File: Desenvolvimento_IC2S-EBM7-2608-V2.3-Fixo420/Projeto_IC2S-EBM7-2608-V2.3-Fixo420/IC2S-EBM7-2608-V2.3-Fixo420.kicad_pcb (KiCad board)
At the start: 4 copper layers, 60 x 60 mm, 148 parts, among them P1 M20-7822046, P2 M20-7821446, T1 TP_+24V, T2 TP_GND_ADC_P1, T3 TP_DGND, T4 TP_+5V_REG, T5 TP_+3.3V_DIG, T6 TP_+3.3V_ANA, T7 TP_GND_ADC, T8 TP_+24V_ADC, U1 R-78HB5.0-0.5L, U10 TPS26613DDFR, U11 TPS26613DDFR, U12 TPS7A4001DGN, U13 LP5907MFX-2.5, U2 MCP1824ST-3302E/DB, U3 SPX3819M5-L-3-3/TR, U4 TL431B, U5 ISO7141CCDBQR, U6 AD7124-8BCPZ, U7 ADR4525BRZ, U8 TPS26613DDFR, U9 TPS26613DDFR

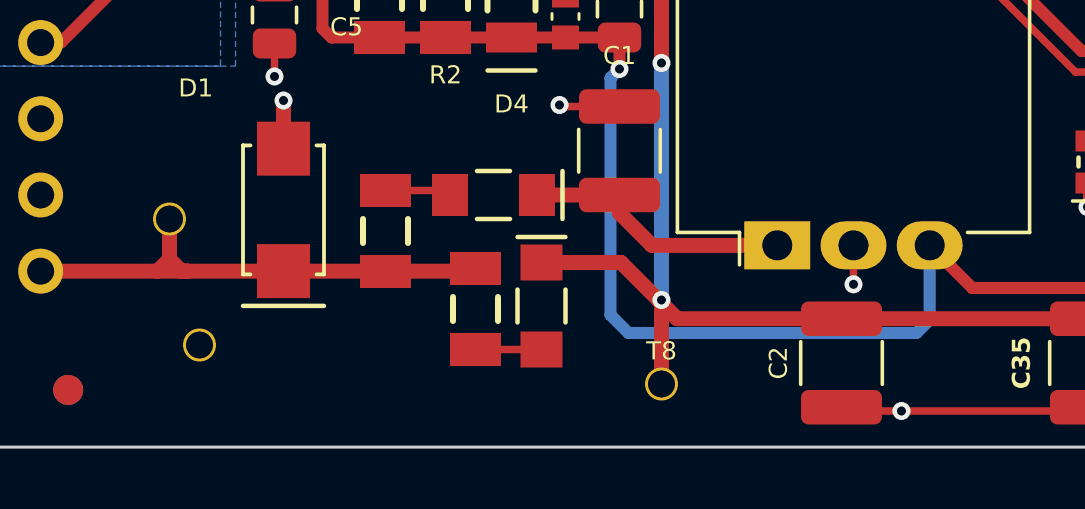
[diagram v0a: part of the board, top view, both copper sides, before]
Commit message: Revisao da reuniao 28-09: ramo unico de 24 V, 100 nF a 50 V, um so MPN de 1 uF
- Saem F2, o diodo e o condensador do ramo +24V_ADC; F1 + diodo alimentam o
  R-78HB e o +24V_ADC. +24V_REG deixa de existir (esquematico, PCB, netclasses).
- Condensador de entrada do R-78HB conferido contra o datasheet Recom (p.4):
  10 uF/100 V cumpre os 3,3 uF/100 V pedidos com Vin > 50 V. Sem alteracao.
- 100 nF fora do 24 V -> TDK C1608X7R1H104K080AA (50 V); o do +24V_ADC fica
  GRM188R72A104KA35D (100 V). 1 uF -> TDK C1608X7R1H105K080AB nos quatro.
- Notas 2, 13 e 14 da folha 2; README e registo em 00-Especificacoes;
  catalogo TDK em Documentos_de_Referencia.

Co-Authored-By: Claude Opus 5.5 (1M context) <noreply@anthropic.com>
Claude-Session: https://claude.ai/code/session_01KPnkiJQKrkjgRqqw9M78ie
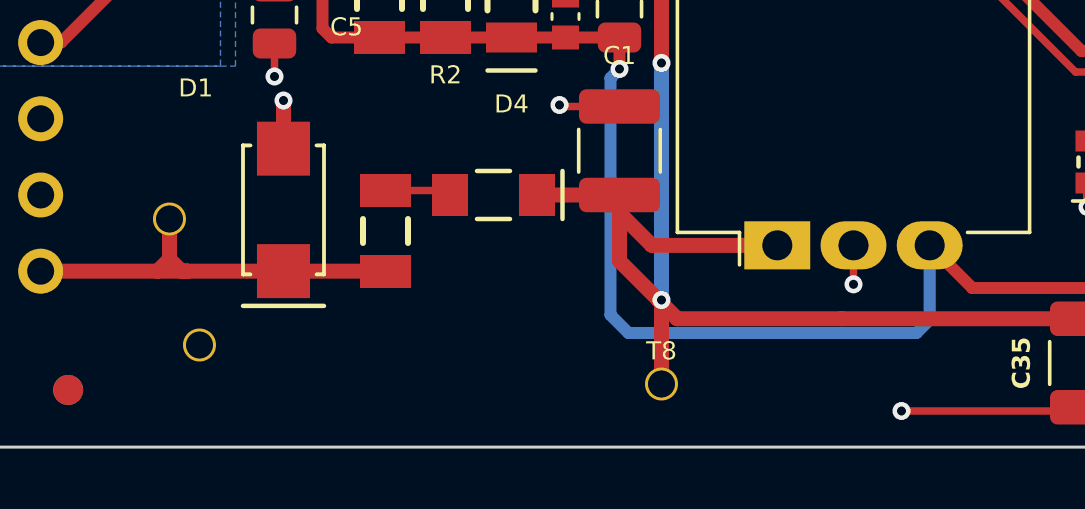
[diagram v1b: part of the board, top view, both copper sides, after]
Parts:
- removed C2: 10uF/100V, EBM7_V23:C_1210_3225Metric
- removed D3: MBR1H100SF, EBM7_V23:SOD123
- removed F2: CC12H750MA-TR, EBM7_V23:1206F
- C10, C12, C13, C18, C19, C20, C23, C24, C26, C27, C28, C29, C30, C31, C32, C33, C37, C39, C4, C40, C42, C43, C44, C9: value 100nF -> 100nF/50V
- C21, C22: value 1uF -> 1uF/50V
- C41, C47: value 1uF/16V -> 1uF/50V
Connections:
- C1 pad 1: +24V_REG -> +24V_ADC
- D2 pad 1: +24V_REG -> +24V_ADC
- U1 pad 1: +24V_REG -> +24V_ADC
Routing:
- net +24V_REG: track 8.88 -> 0.00 mm
- net +24V_ADC: track 110.6 -> 118.5 mm
- net +24V: track 17.8 -> 14.2 mm
- net Net-(D3-A): track 2.20 -> 0.00 mm
- net GND_ADC: track 151.6 -> 149.5 mm

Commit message: NTC com simbolo de termistor e explicacao do TL431 do +3.3V_ANA
- Folha 8: o NTC deixa de usar Device:R e passa a Device:Thermistor_NTC
  (mesmos pinos; netlist e PCB inalterados). Observacao da reuniao de 25-09.
- Documento porque_TL431_*_no_3V3_ANA.md: o LDO nao absorve corrente, os
  BAV199 despejam os surtos no rail e o TL431 segura-o abaixo do maximo
  absoluto do AD7124; numeros tirados dos datasheets locais.

Co-Authored-By: Claude Opus 5.5 (1M context) <noreply@anthropic.com>
Claude-Session: https://claude.ai/code/session_01KPnkiJQKrkjgRqqw9M78ie
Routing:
- net GND_ADC: track 149.5 -> 143.4 mm, vias 69 -> 68
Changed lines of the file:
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@@
-	)
-	(segment
-		(start 155.375 133.8)
-		(end 149.2 133.8)
-		(width 0.25)
-		(layer "F.Cu")
-		(net "GND_ADC")
 	)
 	(segment
@@
 		(size 0.6)
 		(drill 0.3)
-		(layers "F.Cu" "B.Cu")
-		(free yes)
-		(net "GND_ADC")
-	)
-	(via
-		(at 149.2 133.8)
-		(size 0.6)
-		(drill 0.3)

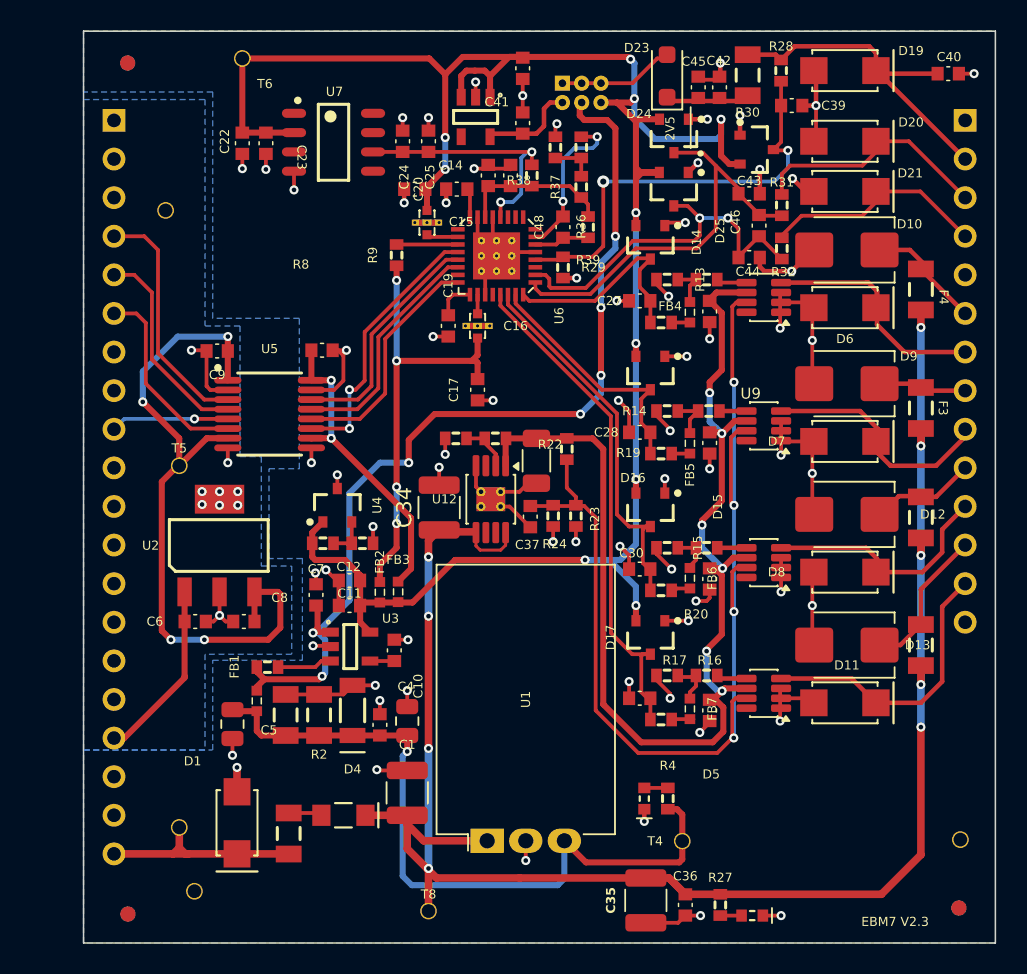
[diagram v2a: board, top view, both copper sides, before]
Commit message: LDO 3,3 V do lado PLC: U2 MCP1824ST (SOT-223) -> SPX3819M5-L-3-3/TR (SOT-23-5), mesmo MPN do U3
- Criterio da equipa: menos MPN, mais pecas do mesmo tipo; o MCP1824ST sai.
- EN a VIN, BYP aberto; estabilidade com ceramico sem garantia no datasheet (provada em campo na V2.2).
- Esquematico: ERC 0; netlist so muda os pinos do U2. PCB: pegada SOT-23-5 no
  mesmo sitio; faltam rotear 6 ligacoes do U2; Gerbers/PnP por regenerar depois.
- Registo: alteracao_LDO_3V3_lado_PLC_2026-09-28.md (comparacao, verificacao e
  riscos em aberto). BOM e PDF do esquematico regenerados.

Co-Authored-By: Claude Opus 5.5 (1M context) <noreply@anthropic.com>
Claude-Session: https://claude.ai/code/session_01KPnkiJQKrkjgRqqw9M78ie
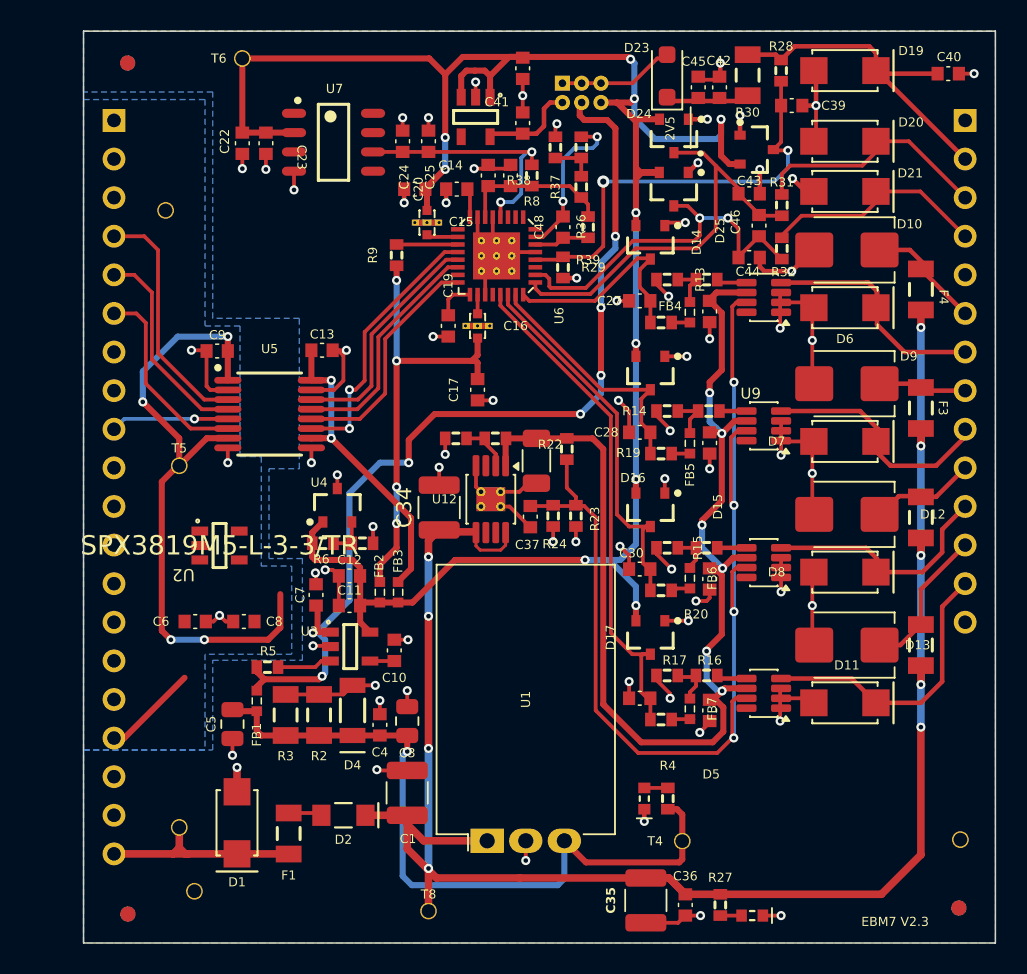
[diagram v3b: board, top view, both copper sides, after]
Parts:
- U2: value MCP1824ST-3302E/DB -> SPX3819M5-L-3-3/TR; footprint EBM7_V23:SOT-223-3 -> EBM7_V23:SOT-23-5
- moved C12 0.30 mm to (136.0, 110.8)
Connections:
- U2 pad 3: +3.3V -> +5V
- U2 pad 4: DGND -> unconnected-(U2-BP-Pad4)
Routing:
- net +5V: track 11.9 -> 6.29 mm
- net +3.3V: track 46.1 -> 42.4 mm
- net DGND: track 9.72 -> 8.02 mm, vias 9 -> 3
- net +3.3V_ANA: track 141.3 -> 141.9 mm

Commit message: C49 2,2 uF na saida do U2 (SPX3819), como a saida do SPX da V2.2 em campo
- Datasheet SPX3819 Fig. 18 (p.8) conferido: EN a VIN e BYP aberto como a figura; saida
  cerâmica 2,2 + 10 uF + 100 nF (V2.2 so tinha ceramicos no SPX). MPN C1608X5R1E225K080AB
  ja na BOM (C7/C11/C46). PCB: clone do C8 a 3 mm do U2, 2 ligacoes por rotear.
- Inclui as alteracoes de roteamento em curso do projectista no PCB.
- ERC 0; DRC 0 erros, sem avisos novos, paridade 0. BOM e PDF regenerados.

Co-Authored-By: Claude Opus 5.5 (1M context) <noreply@anthropic.com>
Claude-Session: https://claude.ai/code/session_01KPnkiJQKrkjgRqqw9M78ie
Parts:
- added C49: 2.2uF, EBM7_V23:0603C, F.Cu at (130.4, 109.8)
- moved U2 0.90 mm to (127.5, 109.8), turned to 90 degrees
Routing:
- net +5V: track 6.29 -> 9.59 mm

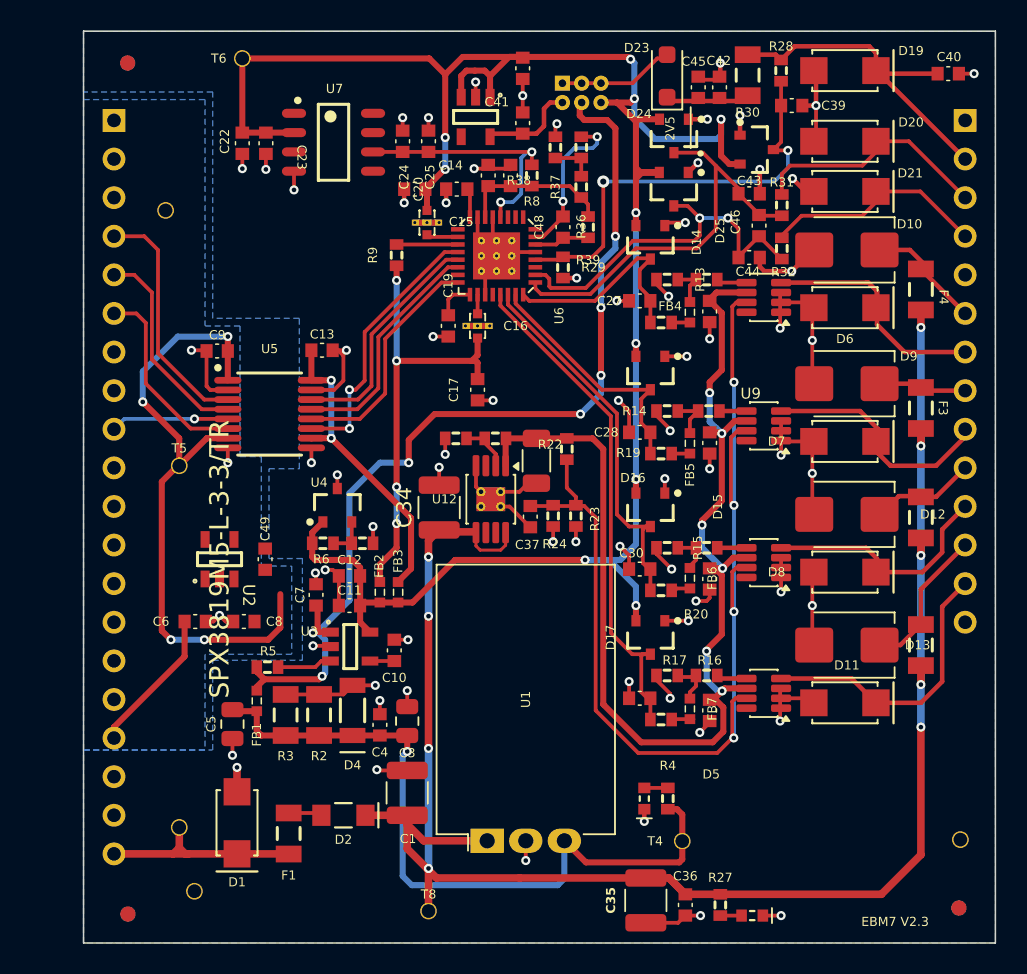
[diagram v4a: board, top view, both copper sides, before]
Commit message: Roteamento do U2 (SPX3819) e do bypass do ISO7141; pacote de fabricacao regenerado
PCB:
- C49 (2,2 uF) e C8 (10 uF) junto do VOUT do U2 (1,68 e 2,23 mm), C6 na
  entrada a 3,0 mm.
- C9 (100 nF) reposto como bypass do VCC1 do U5 (1,93 mm), massa por via
  DGND a 1,0 mm do pad. Tinha sido movido com o grupo do U2 (6,3 mm).
- Rede unconnected-(U2-BP-Pad4) na classe DIGSIDE (pad NC do SPX3819 dentro
  da zona DGND; sem isto a regra de barreira de 1,0 mm disparava contra C9).
- DRC kicad-cli com paridade: 0 erros, 0 avisos, 0 desligados, paridade 0.

Esquematico: sem alteracao electrica (paridade 0, netlist igual). Restauro do
historico local do KiCad: coordenadas arredondadas (02), fios colineares
fundidos com os mesmos extremos (04), rectangulo grafico removido (06),
ordem dos textos (08).

Fabricacao: Gerbers, furacao, PnP, stencil, BOM, vistas, STEP e PDF do
esquematico regenerados desta placa (antes eram de 28-09 02:48).

Co-Authored-By: Claude Opus 5.5 (1M context) <noreply@anthropic.com>
Claude-Session: https://claude.ai/code/session_01KPnkiJQKrkjgRqqw9M78ie
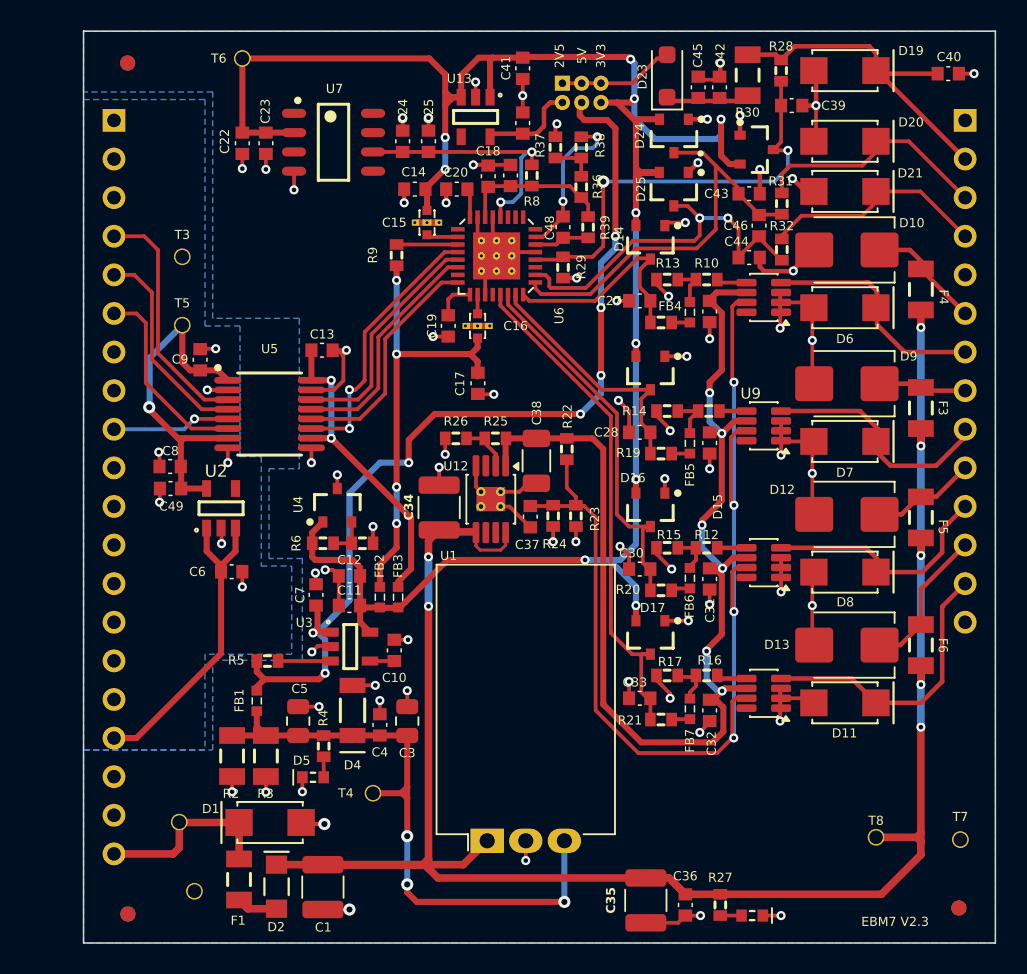
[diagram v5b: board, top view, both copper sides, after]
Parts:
- moved T8 29.8 mm to (170.7, 128.1)
- moved R4 22.9 mm to (134.3, 122.0), turned to -90 degrees
- moved D5 21.8 mm to (133.6, 124.1), turned to 0 degrees
- moved T4 20.6 mm to (137.6, 125.2)
- moved C8 11.3 mm to (124.2, 103.7)
- moved T5 9.25 mm to (125.0, 94.3)
- moved C1 8.32 mm to (134.2, 131.3), turned to -90 degrees
- moved C49 7.77 mm to (124.2, 105.1), turned to 0 degrees
- moved D2 6.44 mm to (131.2, 131.3), turned to 90 degrees
- moved R2 6.33 mm to (128.3, 122.7), turned to -90 degrees
- moved F1 4.45 mm to (128.7, 130.8), turned to -90 degrees
- moved C5 4.33 mm to (132.6, 120.4), turned to -90 degrees
- moved C6 4.06 mm to (128.2, 110.6)
- moved U2 3.35 mm to (127.5, 106.4)
- moved T3 3.24 mm to (125.0, 89.8)
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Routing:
- net +3.3V: track 42.4 -> 23.7 mm, vias 4 -> 1
- net +5V: track 9.59 -> 20.9 mm
- net +24V_ADC: track 118.5 -> 129.0 mm, vias 9 -> 7
- net +5V_REG: track 48.4 -> 42.0 mm, vias 1 -> 3
- net GND_ADC: track 143.8 -> 141.2 mm, vias 68 -> 70
- net +24V: track 14.2 -> 11.6 mm
- net +3.3V_ANA: track 141.9 -> 140.2 mm
- net DGND: track 8.02 -> 7.28 mm, vias 3 -> 7
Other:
- board text added: "3V3"
